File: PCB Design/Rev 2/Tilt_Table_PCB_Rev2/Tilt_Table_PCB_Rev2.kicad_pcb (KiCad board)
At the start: 2 copper layers, 52.1 x 78.3 mm, 74 parts, among them J1 2171750001, J10 X_SERVO_HDR, J11 GPIO_HDR, J12 BUCK_EN, J2 7x1 RECP, J3 PD_Output, J5 BOOT_HDR, J6 USB_B_Micro, J7 SWD, J8 Touch_Panel_HDR, J9 Y_SERVO_HDR, Q1 DMP3098LSD-13, Q3 2N7002, U1 TPS54531DDA, U2 CYPD3177-24LQ, U3 TLV75533PDBV, U4 STM32F042F6Px

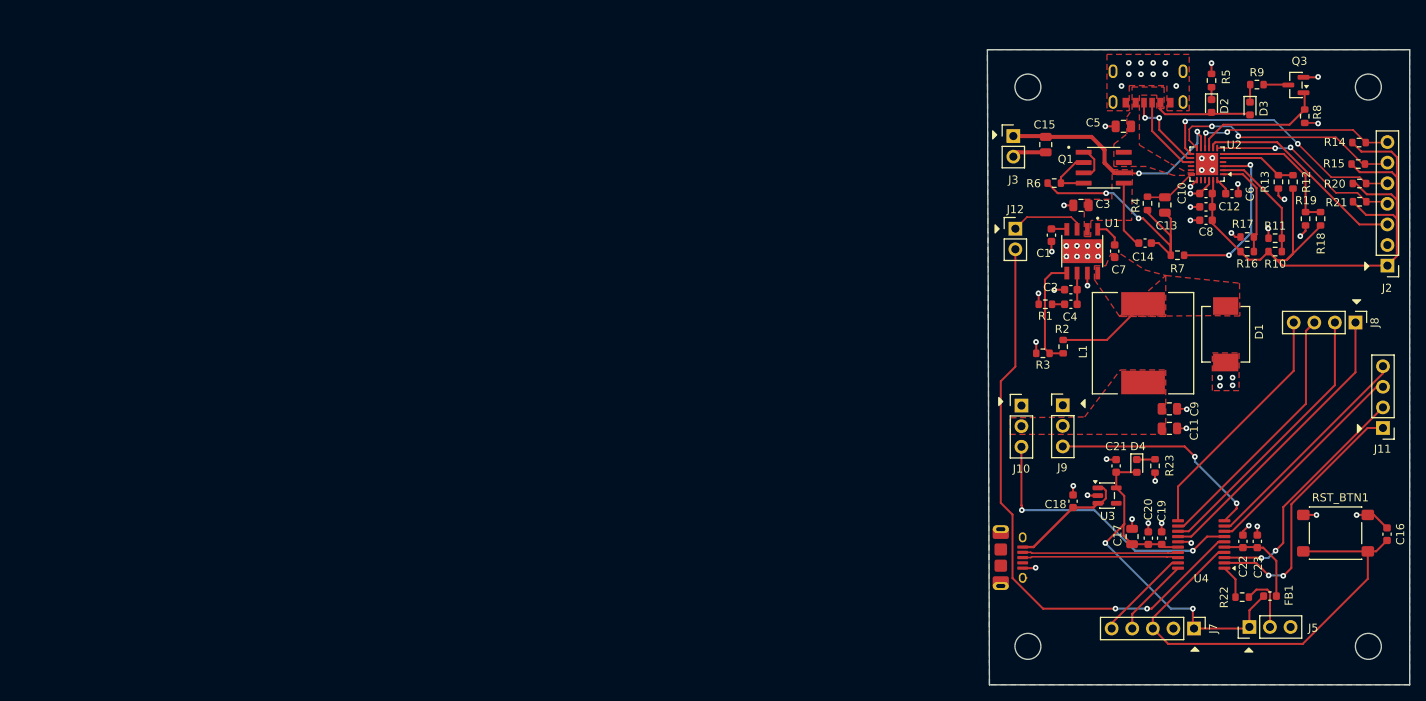
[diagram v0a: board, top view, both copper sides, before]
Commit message: Rev 2 schematic updated
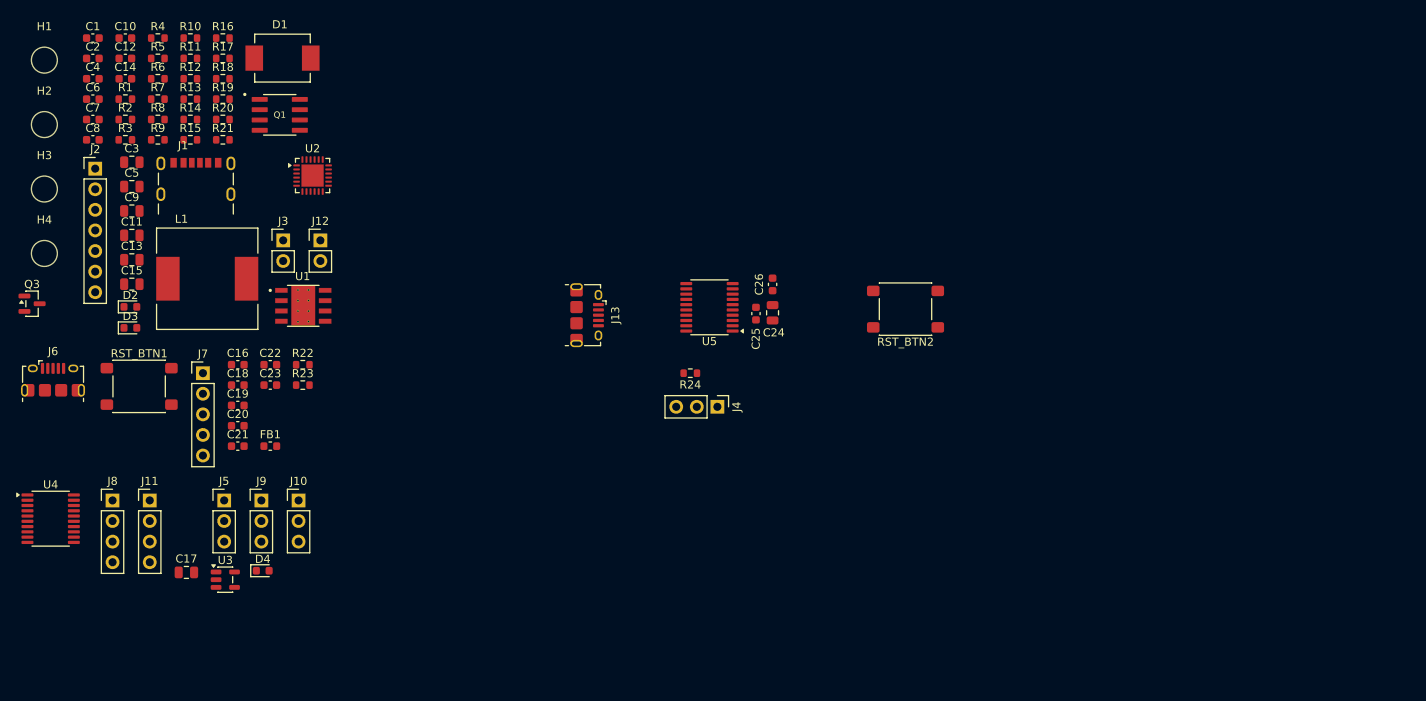
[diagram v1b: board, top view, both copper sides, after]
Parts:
- added C24: 4.7u, Capacitor_SMD:C_0805_2012Metric, F.Cu at (116.5, 57.9)
- added C25: 100n, Capacitor_SMD:C_0603_1608Metric, F.Cu at (114.5, 58.0)
- added C26: 100n, Capacitor_SMD:C_0603_1608Metric, F.Cu at (116.5, 54.4)
- added J13: USB_B_Micro, Connector_USB:USB_Micro-B_Amphenol_10118194-0001LF_Horizontal, F.Cu at (93.6, 58.1)
- added J4: BOOT_HDR, Connector_PinHeader_2.54mm:PinHeader_1x03_P2.54mm_Vertical, F.Cu at (109.7, 69.5)
- added R24: 10k, Resistor_SMD:R_0603_1608Metric, F.Cu at (106.3, 65.3)
- added RST_BTN2: RST_SW, Button_Switch_SMD:SW_SPST_PTS645Sx43SMTR92, F.Cu at (132.9, 57.4)
- added U5: STM32C071FBPx, Package_SO:TSSOP-20_4.4x6.5mm_P0.65mm, F.Cu at (108.7, 57.2)
- R23: value 100 -> 330
- moved H4 170.4 mm to (26.7, 50.5)
- moved H2 163.4 mm to (26.7, 34.6)
- moved J2 159.9 mm to (32.9, 40.1), turned to 0 degrees
- moved Q3 158.2 mm to (25.1, 56.7), turned to 0 degrees
- moved J8 154.9 mm to (35.1, 81.0), turned to 0 degrees
- moved J11 152.4 mm to (39.7, 81.0), turned to 0 degrees
- moved RST_BTN1 148.7 mm to (38.4, 66.9)
- moved R14 144.2 mm to (44.7, 34.0)
- moved R15 144.1 mm to (44.7, 36.5)
- moved C16 143.3 mm to (50.5, 64.3), turned to 0 degrees
- moved U4 142.0 mm to (27.4, 83.2), turned to 0 degrees
- moved R8 141.5 mm to (40.7, 34.0), turned to 0 degrees
- moved C6 141.0 mm to (32.6, 31.5)
- moved D3 140.8 mm to (37.3, 59.7), turned to 0 degrees
- moved R21 140.4 mm to (48.7, 36.5)
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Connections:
- J10 pad 1: GND -> /MCU/SERVO_X
- J10 pad 3: /MCU/SERVO_X -> GND
- J9 pad 1: GND -> /MCU/SERVO_Y
- J9 pad 3: /MCU/SERVO_Y -> GND
- R2 pad 1: /Power/PH -> +6V
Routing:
- net PDC_3.3V: track 103.5 -> 0.00 mm
- net SERVO_EN: track 73.0 -> 0.00 mm, vias 2 -> 0
- net /MCU/NRST: track 58.4 -> 0.00 mm
- net GND: track 54.6 -> 0.00 mm, vias 60 -> 0
- net +3.3V: track 50.0 -> 0.00 mm, vias 2 -> 0
- net /Power/VBUS_OUT: track 39.1 -> 0.00 mm, vias 2 -> 0
- net /MCU/Tilt_Xri: track 36.4 -> 0.00 mm
- net /MCU/SERVO_X: track 35.6 -> 0.00 mm, vias 2 -> 0
- net /Power/VBUS_FET_EN_R: track 35.4 -> 0.00 mm, vias 2 -> 0
- net /MCU/Tilt_Xle: track 34.5 -> 0.00 mm
- net /Power/HPI_SCL: track 32.6 -> 0.00 mm, vias 2 -> 0
- net /MCU/Tilt_Ydown: track 32.5 -> 0.00 mm
- net /MCU/PF0: track 32.4 -> 0.00 mm, vias 2 -> 0
- net /MCU/Tilt_Yup: track 30.4 -> 0.00 mm
- net /MCU/PF1: track 29.9 -> 0.00 mm, vias 2 -> 0
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- removed copper zone on F.Cu, net +6V
- removed copper zone on F.Cu, net /Power/PH
- removed copper zone on F.Cu, net /Power/VBUS_OUT
- removed copper zone on B.Cu, net GND
- removed copper zone on F.Cu, net GND
- removed copper zone on F.Cu, net VBUS_IN
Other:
- board outline removed

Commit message: PCB Rev 2 Update
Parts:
- removed C21, C23: 1u, Capacitor_SMD:C_0603_1608Metric
- removed C22: 10n, Capacitor_SMD:C_0603_1608Metric
- removed C24: 4.7u, Capacitor_SMD:C_0805_2012Metric
- removed C25, C26: 100n, Capacitor_SMD:C_0603_1608Metric
- removed FB1: 600R, Inductor_SMD:L_0603_1608Metric
- removed J12: BUCK_EN, Connector_PinHeader_2.54mm:PinHeader_1x02_P2.54mm_Vertical
- removed J13: USB_B_Micro, Connector_USB:USB_Micro-B_Amphenol_10118194-0001LF_Horizontal
- removed Q3: 2N7002, Package_TO_SOT_SMD:SOT-23
- removed R24: 10k, Resistor_SMD:R_0603_1608Metric
- removed RST_BTN1, RST_BTN2: RST_SW, Button_Switch_SMD:SW_SPST_PTS645Sx43SMTR92
- removed U5: STM32C071FBPx, Package_SO:TSSOP-20_4.4x6.5mm_P0.65mm
- added Q2: 2N7002, Package_TO_SOT_SMD:SOT-23, F.Cu at (154.0, 40.5)
- added SW1: RST_BTN, Button_Switch_SMD:SW_SPST_PTS645Sx43SMTR92, F.Cu at (153.7, 71.0)
- C1: value 10n -> 3.3u; footprint Capacitor_SMD:C_0603_1608Metric -> Capacitor_SMD:C_0805_2012Metric
- C10: value 100n -> 22p; moved to B.Cu
- C11: value 47u -> 10u
- C12: value 100n -> 2200p; moved to B.Cu
- C13, C17: value 4.7u -> 100n; footprint Capacitor_SMD:C_0805_2012Metric -> Capacitor_SMD:C_0603_1608Metric; moved to B.Cu
- C14: value 100n -> 47u; footprint Capacitor_SMD:C_0603_1608Metric -> Capacitor_SMD:C_0805_2012Metric
- C15: value 4.7u -> 47u
- C16: value 100n -> 1u
- C19: value 100n -> 4.7u; footprint Capacitor_SMD:C_0603_1608Metric -> Capacitor_SMD:C_0805_2012Metric; moved to B.Cu
- C2: value 22p -> 1u; moved to B.Cu
- C20: moved to B.Cu
- C3: value 10u -> 1u; footprint Capacitor_SMD:C_0805_2012Metric -> Capacitor_SMD:C_0603_1608Metric; moved to B.Cu
- C4: value 2200p -> 100n; moved to B.Cu
- C5: value 3.3u -> 100n; footprint Capacitor_SMD:C_0805_2012Metric -> Capacitor_SMD:C_0603_1608Metric; moved to B.Cu
- C6, C8: value 1u -> 4.7u; footprint Capacitor_SMD:C_0603_1608Metric -> Capacitor_SMD:C_0805_2012Metric
- C9: value 47u -> 10n; footprint Capacitor_SMD:C_0805_2012Metric -> Capacitor_SMD:C_0603_1608Metric
- D1: value 0.55V -> GREEN; footprint footprints:DIOM7959X262N -> LED_SMD:LED_0603_1608Metric
- D2: value GREEN -> RED
- D3: value RED -> 0.55V; footprint LED_SMD:LED_0603_1608Metric -> footprints:DIOM7959X262N
- J11: value GPIO_HDR -> Touch_Panel_HDR
- J4: value BOOT_HDR -> BUCK_EN; footprint Connector_PinHeader_2.54mm:PinHeader_1x03_P2.54mm_Vertical -> Connector_PinHeader_2.54mm:PinHeader_1x02_P2.54mm_Vertical
- J5: value BOOT_HDR -> MCU_Header; footprint Connector_PinHeader_2.54mm:PinHeader_1x03_P2.54mm_Vertical -> Connector_PinHeader_2.54mm:PinHeader_1x08_P2.54mm_Vertical
- J6: value USB_B_Micro -> BOOT_HDR; footprint Connector_USB:USB_Micro-B_Amphenol_10118194-0001LF_Horizontal -> Connector_PinHeader_2.54mm:PinHeader_1x03_P2.54mm_Vertical
- J8: value Touch_Panel_HDR -> USB_B_Micro; footprint Connector_PinHeader_2.54mm:PinHeader_1x04_P2.54mm_Vertical -> Connector_USB:USB_Micro-B_Amphenol_10118194-0001LF_Horizontal
- R1: value 37.4k -> 5.1k; moved to B.Cu
- R10, R12: value 5.1k -> 2.2k; moved to B.Cu
- R11: value DNP -> 2.2k; moved to B.Cu
- R13: value 5.1k -> 20k
- R16: value 5.1k -> 2.2k
- R17: value DNP -> 100k
- R18: value DNP -> 4.6k
- R19: value 5.1k -> 37.4k; moved to B.Cu
- R2: value 65.7k -> DNP; moved to B.Cu
- R20: value 2.2k -> 65.7k; moved to B.Cu
- R21: value 2.2k -> 10k; moved to B.Cu
- R22: value 10k -> 330
- R23: value 330 -> 10k; moved to B.Cu
- R3: value 10k -> 5.1k; moved to B.Cu
- R4: value 20k -> 5.1k; moved to B.Cu
- R5: value 2.2k -> 5.1k; moved to B.Cu
- R6, R7: value 2.2k -> DNP; moved to B.Cu
- R8: value 100k -> 5.1k; moved to B.Cu
- R9: value 4.6k -> 2.2k; moved to B.Cu
- U1: value TPS54531DDA -> CYPD3177-24LQ; footprint footprints:VREG_LM5017MR_NOPB -> Package_DFN_QFN:QFN-24-1EP_4x4mm_P0.5mm_EP2.75x2.75mm
- U2: value CYPD3177-24LQ -> TPS54531DDA; footprint Package_DFN_QFN:QFN-24-1EP_4x4mm_P0.5mm_EP2.75x2.75mm -> footprints:VREG_LM5017MR_NOPB
- U4: value STM32F042F6Px -> STM32C071FBPx
- moved H4 140.2 mm to (163.6, 80.7)
- moved H2 137.1 mm to (163.6, 28.2)
- moved J6 135.0 mm to (162.8, 67.8)
- moved J2 131.1 mm to (163.7, 49.4), turned to 180 degrees
- moved C1 121.2 mm to (153.7, 30.8), turned to 90 degrees
- moved R9 119.5 mm to (160.2, 34.2)
- moved D2 119.3 mm to (154.4, 34.6), turned to 180 degrees
- moved J11 117.9 mm to (154.8, 55.5), turned to 90 degrees
- moved R12 116.5 mm to (160.2, 44.4)
- moved U4 116.5 mm to (143.2, 70.5), turned to 180 degrees
- moved R11 116.2 mm to (160.1, 39.3)
- moved R10 116.2 mm to (160.1, 36.8)
- moved R3 115.2 mm to (151.4, 47.0), turned to 180 degrees
- moved R4 113.5 mm to (151.4, 48.8)
- moved R1 112.3 mm to (147.8, 48.0), turned to 90 degrees
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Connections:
- C1 pad 1: /Power/SS -> VBUS_IN
- C10 pad 1: PDC_3.3V -> /Power Conversion/COMP
- C11 pad 1: +6V -> VBUS_OUT
- C12 pad 1: PDC_3.3V -> /Power Conversion/COMP
- C12 pad 2: GND -> Net-(C12-Pad2)
- C13 pad 1: VBUS_IN -> /Power Conversion/BOOT
- C13 pad 2: /Power/VBUS_FET_EN_R -> /Power Conversion/PH
- C14 pad 1: /Power/VBUS_OUT -> +6V
- C14 pad 2: /Power/VBUS_FET_EN_R -> GND
- C15 pad 1: /Power/VBUS_OUT -> +6V
- C16 pad 1: /MCU/NRST -> +5V
- C17 pad 1: +3.3V -> /MCU/NRST
- C18 pad 1: +5V -> +3.3V
- C2 pad 1: /Power/COMP -> /Power/PDC_VCCD
- C3 pad 1: /Power/VBUS_OUT -> PDC_3.3V
- C4 pad 1: /Power/COMP -> PDC_3.3V
- C4 pad 2: Net-(C4-Pad2) -> GND
- C5 pad 1: VBUS_IN -> PDC_3.3V
- C6 pad 1: /Power/PDC_VCCD -> VBUS_IN
- C6 pad 2: GND -> /Power/VBUS_FET_EN_R
- C7 pad 1: /Power/BOOT -> VBUS_OUT
- C7 pad 2: /Power/PH -> /Power/VBUS_FET_EN_R
- C8 pad 1: PDC_3.3V -> VBUS_OUT
- C9 pad 1: +6V -> /Power Conversion/SS
- D1 pad 1: /Power/PH -> GND
- D1 pad 2: GND -> Net-(D1-A)
- D3 pad 1: Net-(D3-K) -> /Power Conversion/PH
- D3 pad 2: VBUS_IN -> GND
- J11 pad 1: /MCU/PF0 -> /MCU/Tilt_Xri
- J11 pad 2: /MCU/PF1 -> /MCU/Tilt_Xle
- J11 pad 3: /MCU/UART_TX -> /MCU/Tilt_Ydown
- J11 pad 4: /MCU/UART_RX -> /MCU/Tilt_Yup
- J2 pad 3: /Power/SWD_CLK -> /Power/SWD_IO_INT
- J2 pad 4: /Power/SWD_IO_INT -> /Power/SWD_CLK
- J2 pad 5: /Power/HPI_SCL -> /Power/FLIP
- J2 pad 7: /Power/FLIP -> /Power/HPI_SCL
- J3 pad 1: /Power/VBUS_OUT -> VBUS_OUT
- J4 pad 1: +3.3V -> Net-(J4-Pin_1)
- J4 pad 2: /MCU/SWCLK -> SERVO_EN
- J5 pad 2: /MCU/HDR_BOOT0 -> GND
- J5 pad 3: GND -> /MCU/UART_TX
- J6 pad 1: +5V -> +3.3V
- J6 pad 2: /MCU/USB_D- -> /MCU/SWCLK
- J6 pad 3: /MCU/USB_D+ -> unconnected-(J6-Pin_3-Pad3)
- J8 pad 1: /MCU/Tilt_Xri -> +5V
- J8 pad 2: /MCU/Tilt_Xle -> Net-(J8-D-)
- J8 pad 3: /MCU/Tilt_Ydown -> Net-(J8-D+)
- J8 pad 4: /MCU/Tilt_Yup -> unconnected-(J8-ID-Pad4)
- L1 pad 1: /Power/PH -> /Power Conversion/PH
- Q1 pad 5: /Power/VBUS_OUT -> VBUS_IN
- Q1 pad 6: /Power/VBUS_OUT -> VBUS_IN
- Q1 pad 7: VBUS_IN -> VBUS_OUT
- Q1 pad 8: VBUS_IN -> VBUS_OUT
- R1 pad 1: Net-(C4-Pad2) -> PDC_3.3V
- R1 pad 2: GND -> /Power/VBUS_MAX
- R10 pad 2: /Power/VBUS_MAX -> /Power/HPI_SDA
- R11 pad 1: /Power/VBUS_MAX -> PDC_3.3V
- R11 pad 2: GND -> /Power/FLIP
- R12 pad 2: /Power/ISNK_COARSE -> /Power/SWD_IO_INT
- R13 pad 1: /Power/ISNK_COARSE -> VBUS_IN
- R13 pad 2: GND -> /Power/VBUS_FET_EN_R
- R14 pad 1: PDC_3.3V -> /Power/VBUS_FET_G
- R14 pad 2: /Power/FLIP -> /Power/VBUS_FET_EN_R
- R15 pad 1: PDC_3.3V -> /Power/VBUS_FET_EN_R
- R15 pad 2: /Power/HPI_SDA -> /Power/VBUS_FET_EN
- R16 pad 1: PDC_3.3V -> VBUS_IN
- R16 pad 2: /Power/VBUS_MIN -> Net-(D1-A)
- R17 pad 1: /Power/VBUS_MIN -> /Power/FAULT
- R18 pad 1: PDC_3.3V -> Net-(D2-K)
- R18 pad 2: /Power/ISNK_FINE -> Net-(Q2-D)
- R19 pad 1: /Power/ISNK_FINE -> Net-(C12-Pad2)
- R2 pad 1: +6V -> /Power/VBUS_MAX
- R2 pad 2: /Power/VSENSE -> GND
- R20 pad 1: PDC_3.3V -> +6V
- R20 pad 2: /Power/HPI_SCL -> /Power Conversion/VSENSE
- R21 pad 1: PDC_3.3V -> /Power Conversion/VSENSE
- R21 pad 2: /Power/SWD_IO_INT -> GND
- R22 pad 1: /MCU/HDR_BOOT0 -> Net-(D4-K)
- R22 pad 2: /MCU/BOOT0 -> GND
- R23 pad 1: Net-(D4-K) -> /MCU/SWCLK
- R3 pad 1: /Power/VSENSE -> PDC_3.3V
- R3 pad 2: GND -> /Power/ISNK_COARSE
- R4 pad 1: VBUS_IN -> /Power/ISNK_COARSE
- R4 pad 2: /Power/VBUS_FET_EN_R -> GND
- R5 pad 1: Net-(D2-K) -> PDC_3.3V
- R5 pad 2: GND -> /Power/VBUS_MIN
- R6 pad 1: /Power/VBUS_FET_G -> /Power/VBUS_MIN
- R6 pad 2: /Power/VBUS_FET_EN_R -> GND
- R7 pad 1: /Power/VBUS_FET_EN_R -> PDC_3.3V
- R7 pad 2: /Power/VBUS_FET_EN -> /Power/ISNK_FINE
- R8 pad 1: /Power/FAULT -> /Power/ISNK_FINE
- R9 pad 1: Net-(D3-K) -> PDC_3.3V
- R9 pad 2: Net-(Q3-D) -> /Power/HPI_SCL
- U1 pad 1: /Power/BOOT -> /Power/VBUS_MIN
- U1 pad 10: GND -> /Power/FLIP
- U1 pad 11: GND -> VBUS_OUT
- U1 pad 12: GND -> /Power/HPI_SDA
- U1 pad 13: GND -> /Power/HPI_SCL
- U1 pad 14: GND -> /Power/USB_CC2
- U1 pad 15: GND -> /Power/USB_CC1
- U1 pad 16: (no net) -> unconnected-(U1-NC-Pad16)
- U1 pad 17: (no net) -> unconnected-(U1-NC-Pad17)
- U1 pad 2: /Power/VBUS_OUT -> /Power/VBUS_MAX
- U1 pad 3: Net-(J12-Pin_1) -> /Power/VBUS_FET_EN
- U1 pad 4: /Power/SS -> unconnected-(U1-SAFE_PWR_EN-Pad4)
- U1 pad 5: /Power/VSENSE -> /Power/ISNK_COARSE
- U1 pad 6: /Power/COMP -> /Power/ISNK_FINE
- U1 pad 7: GND -> /Power/SWD_IO_INT
- U1 pad 8: /Power/PH -> /Power/SWD_CLK
- U1 pad 9: GND -> /Power/FAULT
- U2 pad 1: /Power/VBUS_MIN -> /Power Conversion/BOOT
- U2 pad 10: /Power/FLIP -> GND
- U2 pad 11: /Power/VBUS_OUT -> GND
- U2 pad 12: /Power/HPI_SDA -> GND
- U2 pad 13: /Power/HPI_SCL -> GND
- U2 pad 14: /Power/USB_CC2 -> GND
- U2 pad 15: /Power/USB_CC1 -> GND
- U2 pad 16: unconnected-(U2-NC-Pad16) -> (no net)
- U2 pad 17: unconnected-(U2-NC-Pad17) -> (no net)
- U2 pad 2: /Power/VBUS_MAX -> VBUS_OUT
- U2 pad 3: /Power/VBUS_FET_EN -> Net-(J4-Pin_1)
- U2 pad 4: unconnected-(U2-SAFE_PWR_EN-Pad4) -> /Power Conversion/SS
- U2 pad 5: /Power/ISNK_COARSE -> /Power Conversion/VSENSE
- U2 pad 6: /Power/ISNK_FINE -> /Power Conversion/COMP
- U2 pad 7: /Power/SWD_IO_INT -> GND
- U2 pad 8: /Power/SWD_CLK -> /Power Conversion/PH
- U2 pad 9: /Power/FAULT -> GND
- U4 pad 1: /MCU/BOOT0 -> /MCU/UART_RX
- U4 pad 10: /MCU/SERVO_Y -> /MCU/Tilt_Xri
- U4 pad 11: /MCU/Tilt_Yup -> /MCU/SERVO_Y
- U4 pad 12: /MCU/Tilt_Ydown -> /MCU/SERVO_X
- U4 pad 13: /MCU/Tilt_Xle -> SERVO_EN
- U4 pad 14: /MCU/Tilt_Xri -> /MCU/PA7
- U4 pad 15: GND -> /MCU/PA8
- U4 pad 16: +3.3V -> Net-(J8-D-)
- U4 pad 17: /MCU/USB_D- -> Net-(J8-D+)
- U4 pad 18: /MCU/USB_D+ -> /MCU/SWDIO
- U4 pad 19: /MCU/SWDIO -> /MCU/SWCLK
- U4 pad 2: /MCU/PF0 -> /MCU/UART_TX
- U4 pad 20: /MCU/SWCLK -> /MCU/PB3/4/5/6
- U4 pad 3: /MCU/PF1 -> /MCU/PC15
- U4 pad 4: /MCU/NRST -> +3.3V
- U4 pad 5: +3.3VA -> GND
- U4 pad 6: SERVO_EN -> /MCU/NRST
- U4 pad 7: /MCU/SERVO_X -> /MCU/Tilt_Yup
- U4 pad 8: /MCU/UART_TX -> /MCU/Tilt_Ydown
- U4 pad 9: /MCU/UART_RX -> /MCU/Tilt_Xle
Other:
- board outline added: 47 x 60 mm
- copper layers 2 -> 4

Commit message: PCB Rev 2 Update
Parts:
- moved R1 12.7 mm to (151.4, 35.8), turned to 180 degrees
- moved R2 11.9 mm to (151.5, 37.5), turned to 0 degrees
- moved R6 11.4 mm to (151.5, 41.0), turned to 0 degrees
- moved R5 11.3 mm to (151.5, 39.3), turned to 180 degrees
- moved C7 4.21 mm to (133.8, 40.5), turned to -90 degrees
- moved R23 4.00 mm to (159.3, 71.2)
- moved R13 3.20 mm to (134.2, 28.4), turned to 0 degrees
- moved C6 3.00 mm to (134.2, 30.6), turned to 0 degrees
- moved C17 2.95 mm to (156.3, 78.0)
- moved R15 2.40 mm to (137.8, 43.5)
- moved R14 1.90 mm to (135.9, 40.5), turned to -90 degrees
- moved C8 1.81 mm to (128.1, 37.4)
- moved D2 1.64 mm to (156.0, 35.2)
- moved R17 1.64 mm to (156.0, 44.1)
- moved R18 1.64 mm to (156.0, 37.6), turned to 180 degrees
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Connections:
- net Net-(J8-D+) renamed /MCU/USB_D+
- net Net-(J8-D-) renamed /MCU/USB_D-
- J5 pad 3: /MCU/UART_TX -> /MCU/PA7
- J5 pad 4: /MCU/UART_RX -> /MCU/PA8
- J5 pad 5: /MCU/PA7 -> /MCU/PB3/4/5/6
- J5 pad 6: /MCU/PA8 -> /MCU/PC15
- J5 pad 7: /MCU/PC15 -> /MCU/UART_TX
- J5 pad 8: /MCU/PB3/4/5/6 -> /MCU/UART_RX
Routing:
- net GND: track 0.00 -> 37.4 mm, vias 0 -> 49
- net VBUS_IN: track 0.00 -> 23.0 mm, vias 0 -> 12
- net /Power/HPI_SCL: track 0.00 -> 19.5 mm, vias 0 -> 1
- net /Power/HPI_SDA: track 0.00 -> 19.5 mm, vias 0 -> 1
- net /Power/VBUS_FET_EN_R: track 0.00 -> 18.1 mm
- net VBUS_OUT: track 0.00 -> 18.1 mm, vias 0 -> 6
- net /Power/FLIP: track 0.00 -> 16.8 mm, vias 0 -> 1
- net /Power/SWD_IO_INT: track 0.00 -> 16.5 mm, vias 0 -> 1
- net /Power/SWD_CLK: track 0.00 -> 16.1 mm, vias 0 -> 2
- net /MCU/USB_D-: track 0.00 -> 15.7 mm
- net /MCU/USB_D+: track 0.00 -> 15.7 mm
- net PDC_3.3V: track 0.00 -> 14.8 mm, vias 0 -> 9
- net /Power/VBUS_FET_G: track 0.00 -> 13.1 mm
- net /MCU/SERVO_X: track 0.00 -> 12.8 mm, vias 0 -> 1
- net Net-(J4-Pin_1): track 0.00 -> 12.7 mm, vias 0 -> 2
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- added copper zone on F.Cu, net +3.3V
- added copper zone on In2.Cu, net +3.3V
- added copper zone on F.Cu, net +6V
- added copper zone on In2.Cu, net +6V
- added copper zone on F.Cu, net /Power Conversion/PH
- added copper zone on In2.Cu, net /Power Conversion/PH
- added copper zone on F.Cu, net /Power/FET_SRC
- added copper zone on F.Cu, net GND
- added copper zone on In1.Cu, net GND
- added copper zone on In2.Cu, net PDC_3.3V
- added copper zone on F.Cu, net VBUS_IN
- added copper zone on In2.Cu, net VBUS_IN
- added copper zone on F.Cu, net VBUS_OUT
- added copper zone on In2.Cu, net VBUS_OUT

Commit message: PCB Rev 2 Layout Complete - Prior to PCB Order
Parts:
- removed J7: SWD, Connector_PinHeader_2.54mm:PinHeader_1x05_P2.54mm_Vertical
- added J12: SWD, Connector_PinHeader_2.54mm:PinHeader_1x03_P2.54mm_Vertical, F.Cu at (130.6, 81.2)
- C17, C19, C20: moved to F.Cu
- J5: value MCU_Header -> GPIO Header
- J6: value BOOT_HDR -> Boot Mode
- moved D4 19.5 mm to (147.3, 63.0)
- moved R22 19.5 mm to (149.3, 63.0)
- moved C17 9.67 mm to (153.8, 68.6), turned to -90 degrees
- moved J6 7.92 mm to (156.9, 73.9), turned to 90 degrees
- moved Reset 7.89 mm to (159.9, 65.5), turned to 0 degrees
- moved R23 5.43 mm to (160.2, 76.5), turned to 0 degrees
- moved J5 5.23 mm to (139.2, 81.9)
- moved C18 1.42 mm to (135.2, 69.0)
- moved U3 1.42 mm to (131.8, 69.0)
- moved C16 1.08 mm to (128.6, 69.1)
- moved J10 0.80 mm to (129.3, 62.8)
- moved C19 0.62 mm to (150.7, 71.5)
- moved C20 0.50 mm to (148.6, 71.7)
- moved J3 0.15 mm to (124.6, 35.7)
- renumbered SW1 to Reset
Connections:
- J5 pad 3: /MCU/PA7 -> /MCU/PB3/4/5/6
- J5 pad 5: /MCU/PB3/4/5/6 -> /MCU/PA7
- J5 pad 7: /MCU/UART_TX -> /MCU/UART_RX
- J5 pad 8: /MCU/UART_RX -> /MCU/UART_TX
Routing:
- net /MCU/NRST: track 0.00 -> 38.9 mm, vias 0 -> 2
- net /MCU/SWCLK: track 0.00 -> 34.7 mm, vias 0 -> 1
- net SERVO_EN: track 0.00 -> 25.8 mm, vias 0 -> 1
- net /MCU/Tilt_Yup: track 0.00 -> 25.0 mm, vias 0 -> 1
- net /MCU/Tilt_Ydown: track 0.00 -> 19.5 mm, vias 0 -> 1
- net /MCU/Tilt_Xle: track 0.00 -> 17.6 mm, vias 0 -> 1
- net /MCU/PA7: track 0.00 -> 16.1 mm
- net /MCU/Tilt_Xri: track 0.00 -> 15.4 mm, vias 0 -> 1
- net /MCU/UART_TX: track 0.00 -> 14.7 mm
- net /MCU/PA8: track 0.00 -> 14.4 mm
- net /MCU/PC15: track 0.00 -> 13.0 mm
- net /MCU/UART_RX: track 0.00 -> 11.9 mm
- net /MCU/SWDIO: track 0.00 -> 10.9 mm
- net GND: track 37.4 -> 47.5 mm, vias 49 -> 59
- net /MCU/PB3/4/5/6: track 0.00 -> 9.64 mm
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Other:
- board text added: "+20V"
- board text added: "+6V"
- board text added: "3.3V"
- board text added: "GND"
- board text added: "MCU Header"
- board text added: "NRST"
- board text added: "PA7"
- board text added: "PA8"
- board text added: "PB3-6"
- board text added: "PC15"
- board text added: "PCB Edge"
- board text added: "PD Interface"
- board text added: "PD Out"
- board text added: "RX"
- board text added: "SERVO EN"
- board text added: "SERVO_X"
- board text added: "SERVO_Y"
- board text added: "SWCLK"
- board text added: "SWDIO"
- board text added: "Servo X"
- board text added: "Servo Y"
- board text added: "TX"
- board text added: "Touch Plate"
- board text added: "Xle"
- board text added: "Xri"
- board text added: "Ydown"
- board text added: "Yup"
